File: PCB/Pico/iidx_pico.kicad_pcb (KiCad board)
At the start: 2 copper layers, 180 x 160 mm, 77 parts, among them J1 Spin, J2 Spin, J3 RGB, J4 RGB, J5 Spin, J6 Spin, SW1 SWITCH_SPST, SW10 SWITCH_SPST, SW11 SWITCH_SPST, SW12 Tact_4pin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

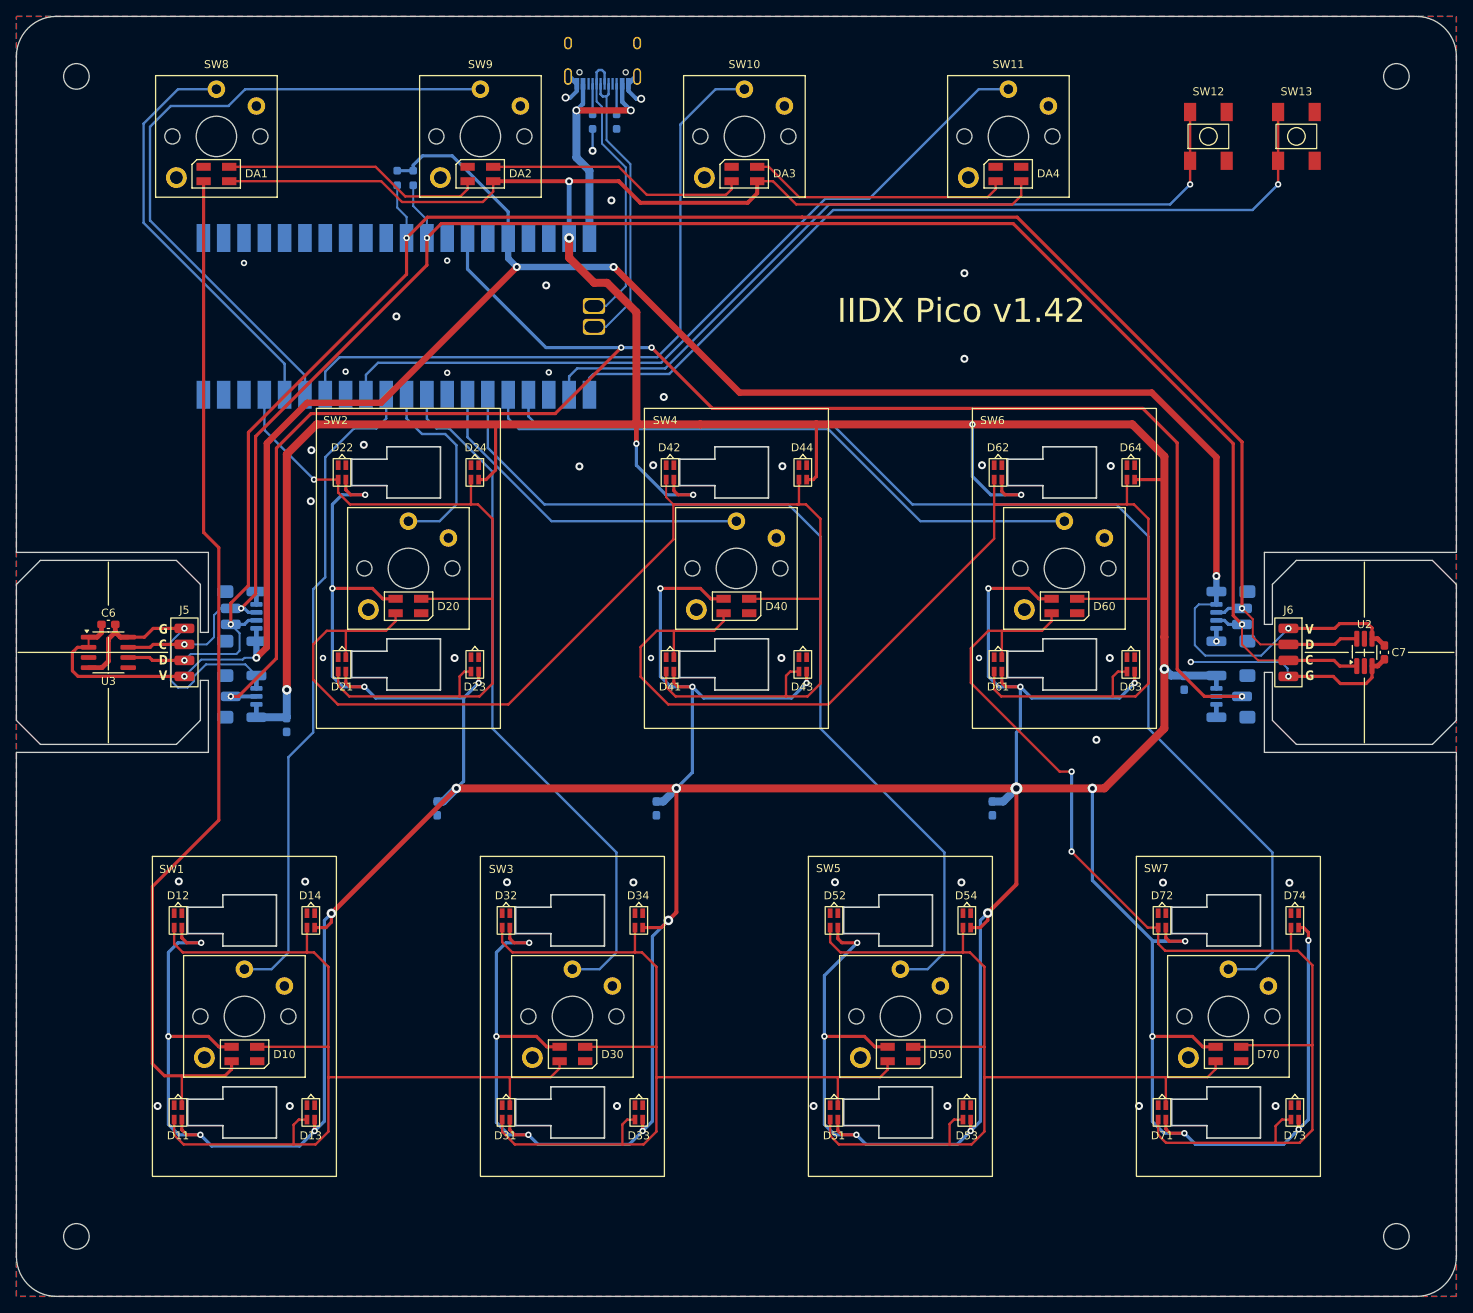
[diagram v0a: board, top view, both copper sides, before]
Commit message: Hall effect switch support
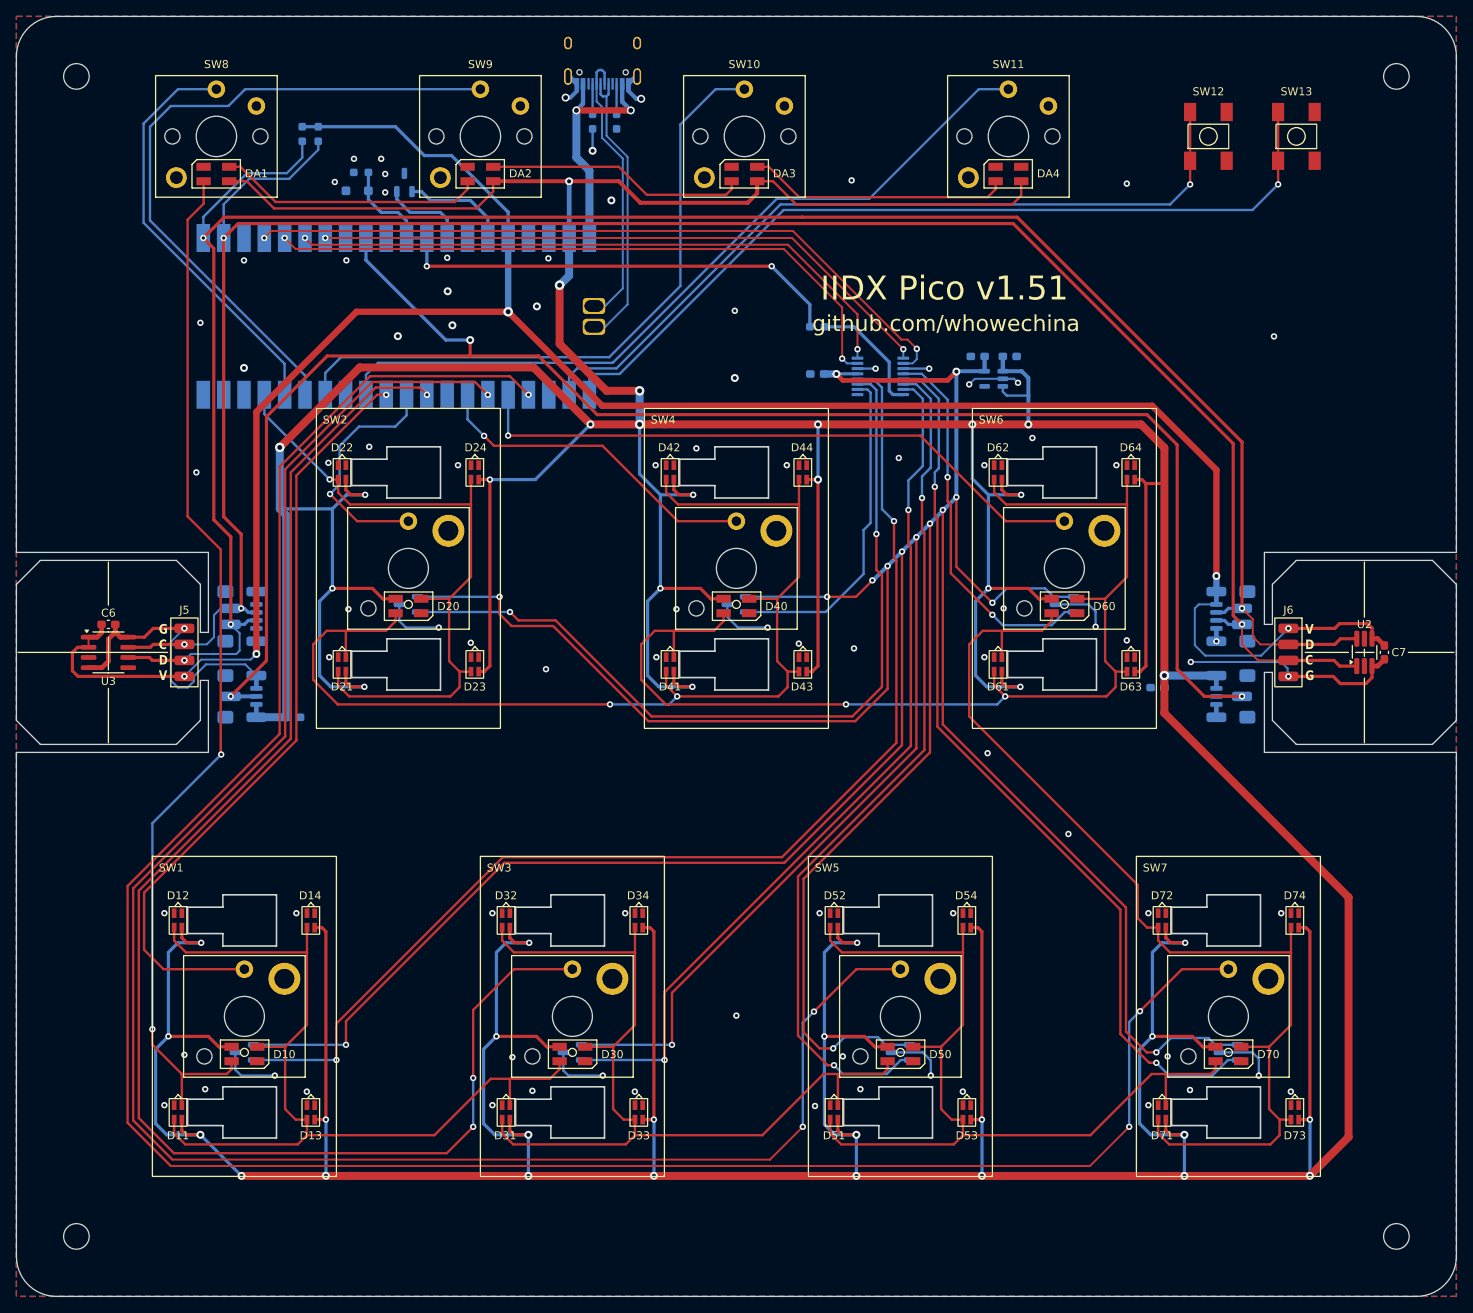
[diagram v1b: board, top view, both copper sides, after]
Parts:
- added C10: 0.1uF, Capacitor_SMD:C_0603_1608Metric_Pad1.08x0.95mm_HandSolder, B.Cu at (147.4, 64.1)
- added C8: 0.1uF, Capacitor_SMD:C_0603_1608Metric_Pad1.08x0.95mm_HandSolder, B.Cu at (171.5, 61.9)
- added C9: 0.1uF, Capacitor_SMD:C_0603_1608Metric_Pad1.08x0.95mm_HandSolder, B.Cu at (167.5, 61.9)
- added H1: SS49E_SOT23, iidx_pico:SOT-23-FAT, B.Cu at (75.8, 148.9)
- added H2: SS49E_SOT23, iidx_pico:SOT-23-FAT, B.Cu at (96.3, 92.9)
- added H3: SS49E_SOT23, iidx_pico:SOT-23-FAT, B.Cu at (116.8, 148.9)
- added H4: SS49E_SOT23, iidx_pico:SOT-23-FAT, B.Cu at (137.3, 92.9)
- added H5: SS49E_SOT23, iidx_pico:SOT-23-FAT, B.Cu at (157.8, 148.9)
- added H6: SS49E_SOT23, iidx_pico:SOT-23-FAT, B.Cu at (178.3, 92.9)
- added H7: SS49E_SOT23, iidx_pico:SOT-23-FAT, B.Cu at (198.8, 148.9)
- added R5: 2K, Resistor_SMD:R_0603_1608Metric_Pad0.98x0.95mm_HandSolder, B.Cu at (147.4, 58.2)
- added R6: 10K, Resistor_SMD:R_0603_1608Metric_Pad0.98x0.95mm_HandSolder, B.Cu at (90.4, 38.9)
- added U4: ADG708BRUZ, Package_SO:TSSOP-16_4.4x5mm_P0.65mm, B.Cu at (155.3, 64.4)
- added U5: LM4040DBZ-3, iidx_pico:SOT-23-FAT, B.Cu at (95.8, 40.2)
- added U6: LP5907MFX-4.5, Package_TO_SOT_SMD:SOT-23-5, B.Cu at (169.5, 64.7)
- added Z1: 3.3V, Diode_SMD:D_SOD-123F, B.Cu at (89.9, 41.2)
- R3, R4: value 4.7K -> 5.1K
- SW1, SW2, SW3, SW4, SW5, SW6, SW7: footprint iidx_pico:SW_Kailh_Choc_V1V2_IIDX -> iidx_pico:SW_Kailh_Choc_HE_IIDX
- moved C3 63.6 mm to (127.5, 70.4), turned to 0 degrees
- moved C4 53.4 mm to (154.6, 164.3), turned to 0 degrees
- moved C5 47.4 mm to (88.3, 164.3), turned to 0 degrees
- moved R3 13.1 mm to (85.0, 34.1)
- moved R4 13.1 mm to (83.0, 34.1)
- moved C2 3.39 mm to (190.0, 103.3), turned to 180 degrees
- moved C1 1.27 mm to (81.9, 107.0), turned to 0 degrees
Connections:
- U1 pad 21: unconnected-(U1-GPIO16-Pad21) -> /SDA
- U1 pad 22: unconnected-(U1-GPIO17-Pad22) -> /SCL
- U1 pad 24: unconnected-(U1-GPIO18-Pad24) -> /EN
- U1 pad 25: unconnected-(U1-GPIO19-Pad25) -> /A2
- U1 pad 26: unconnected-(U1-GPIO20-Pad26) -> /A1
- U1 pad 27: unconnected-(U1-GPIO21-Pad27) -> /A0
- U1 pad 29: unconnected-(U1-GPIO22-Pad29) -> /TT_LED
- U1 pad 31: /SDA -> Net-(U1-GPIO26_ADC0)
- U1 pad 32: /SCL -> Net-(U1-GPIO26_ADC0)
- U1 pad 34: /TT_LED -> unconnected-(U1-GPIO28_ADC2-Pad34)
- U1 pad 35: unconnected-(U1-ADC_VREF-Pad35) -> Net-(U1-ADC_VREF)
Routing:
- net Vref: track 0.00 -> 568.6 mm, vias 0 -> 16
- net /S5: track 0.00 -> 148.1 mm, vias 0 -> 2
- net Net-(U1-GPIO2): track 152.1 -> 284.3 mm, vias 0 -> 3
- net Net-(U1-GPIO4): track 118.5 -> 235.2 mm, vias 0 -> 3
- net /S2: track 0.00 -> 112.3 mm, vias 0 -> 2
- net /S4: track 0.00 -> 109.6 mm, vias 0 -> 2
- net /S3: track 0.00 -> 107.6 mm, vias 0 -> 2
- net /S6: track 0.00 -> 105.1 mm, vias 0 -> 2
- net Net-(U1-GPIO6): track 87.7 -> 184.5 mm, vias 0 -> 3
- net /EN: track 0.00 -> 91.2 mm, vias 0 -> 2
- net /A2: track 0.00 -> 81.8 mm, vias 0 -> 2
- net /A0: track 0.00 -> 79.1 mm, vias 0 -> 2
- net /A1: track 0.00 -> 78.5 mm, vias 0 -> 2
- net GND: track 83.1 -> 157.2 mm, vias 48 -> 88
- net Net-(U1-GPIO26_ADC0): track 0.00 -> 70.1 mm, vias 0 -> 2
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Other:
- board text added: "IIDX Pico v1.51"
- board text added: "github.com/whowechina"
- board text removed: "IIDX Pico v1.42"

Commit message: Pico PCB v1.52, clearance for stab steel
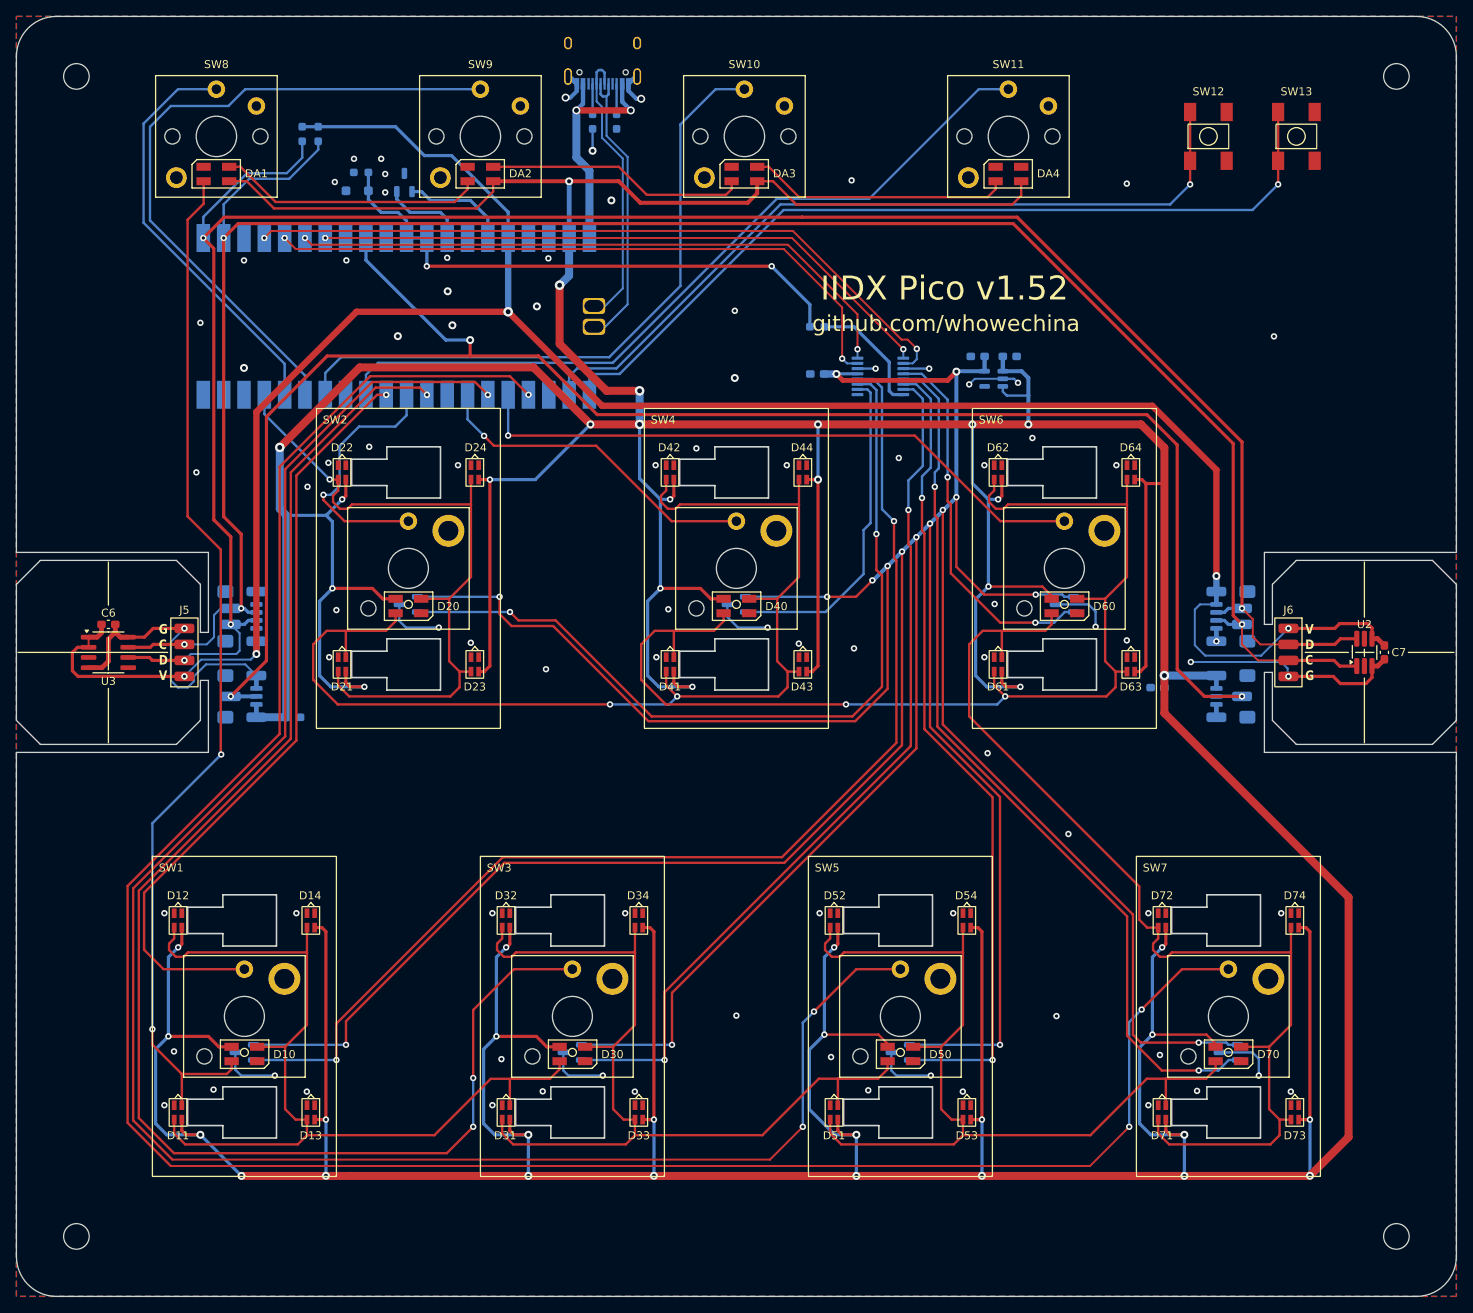
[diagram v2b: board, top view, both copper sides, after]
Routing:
- net +5V: track 1199.6 -> 1169.3 mm
- net Vref: track 568.6 -> 560.3 mm
- net /S3: track 107.6 -> 101.3 mm
- net /LED7: track 131.1 -> 133.4 mm
- net Net-(U1-GPIO7): track 30.2 -> 32.4 mm
- net /LED2: track 85.3 -> 87.3 mm
- net /LED6: track 136.7 -> 138.8 mm
- net /LED4: track 136.7 -> 138.8 mm
- net /LED1: track 110.0 -> 112.1 mm
- net /LED3: track 110.6 -> 112.1 mm
- net /LED5: track 110.6 -> 112.1 mm
- net /S2: track 112.3 -> 111.3 mm
- net GND: track 157.2 -> 157.4 mm, vias 88 -> 89
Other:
- board text added: "IIDX Pico v1.52"
- board text removed: "IIDX Pico v1.51"

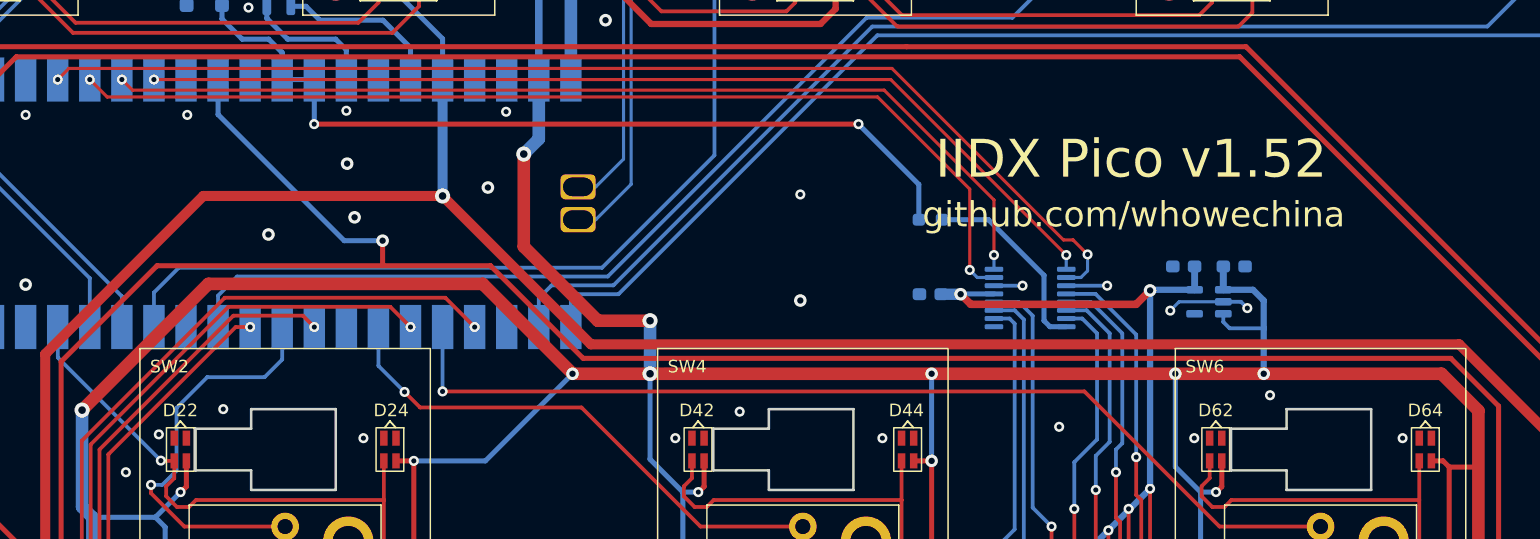
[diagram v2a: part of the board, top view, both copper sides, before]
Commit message: PCB Pico v1.53 (vref from vbus)
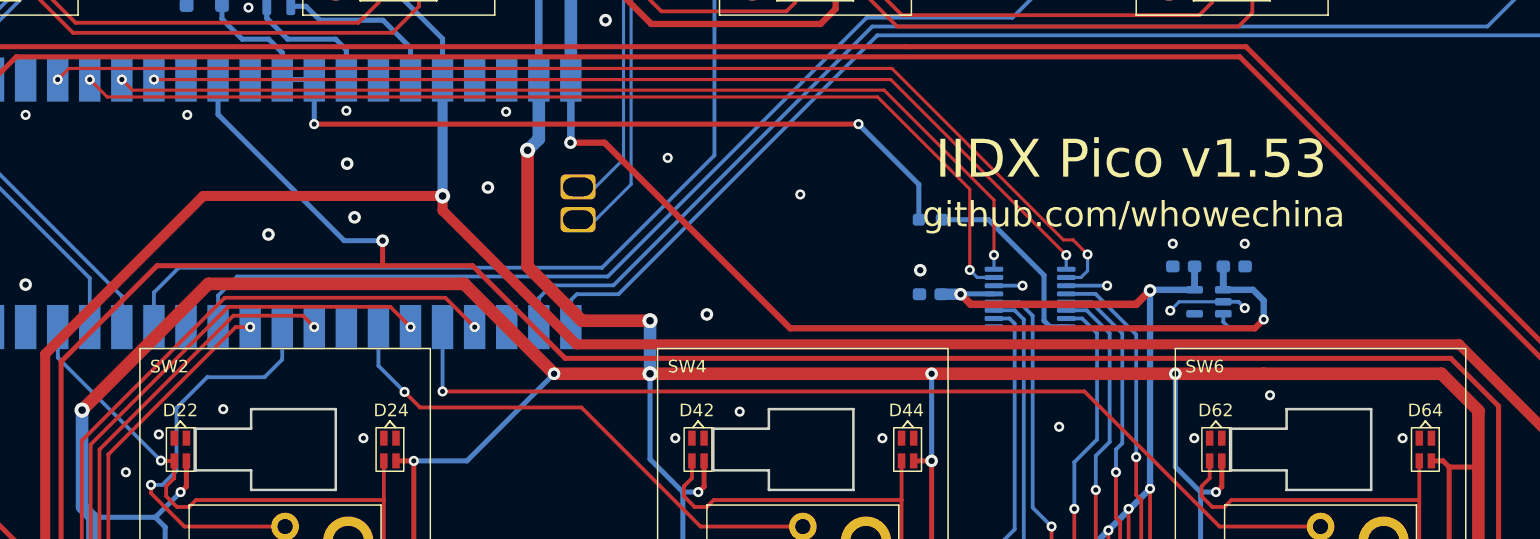
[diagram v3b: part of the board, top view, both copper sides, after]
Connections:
- C8 pad 1: +5V -> VBUS
- U6 pad 1: +5V -> VBUS
- U6 pad 3: +5V -> VBUS
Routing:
- net VBUS: track 31.8 -> 109.2 mm, vias 2 -> 4
- net +5V: track 1169.3 -> 1153.1 mm, vias 45 -> 44
- net +3.3V: track 294.7 -> 295.4 mm
- net GND: track 157.4 -> 157.2 mm, vias 89 -> 93
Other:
- board text added: "IIDX Pico v1.53"
- board text removed: "IIDX Pico v1.52"
